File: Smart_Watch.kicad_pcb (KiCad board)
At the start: 4 copper layers, 32 x 32 mm, 52 parts, among them J1 2169900001, J2 Conn_01x02, J3 Conn_01x06, J4 Conn_01x02, SW2 SW_Push, SW3 SW_Push, SW4 SW_Push, SW5 SW_Push, SW6 SW_Push, SW7 SW_Push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

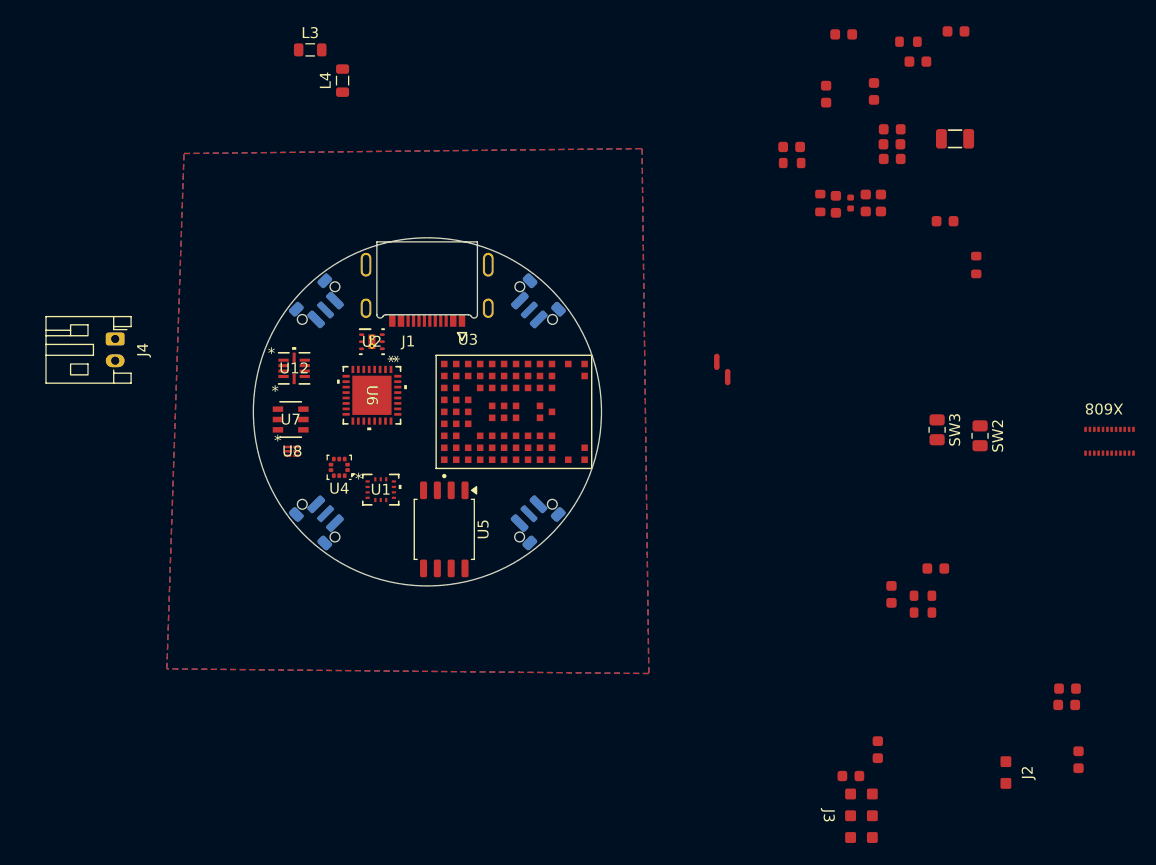
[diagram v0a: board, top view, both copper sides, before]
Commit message: Added Backpack Integration + Layout V1
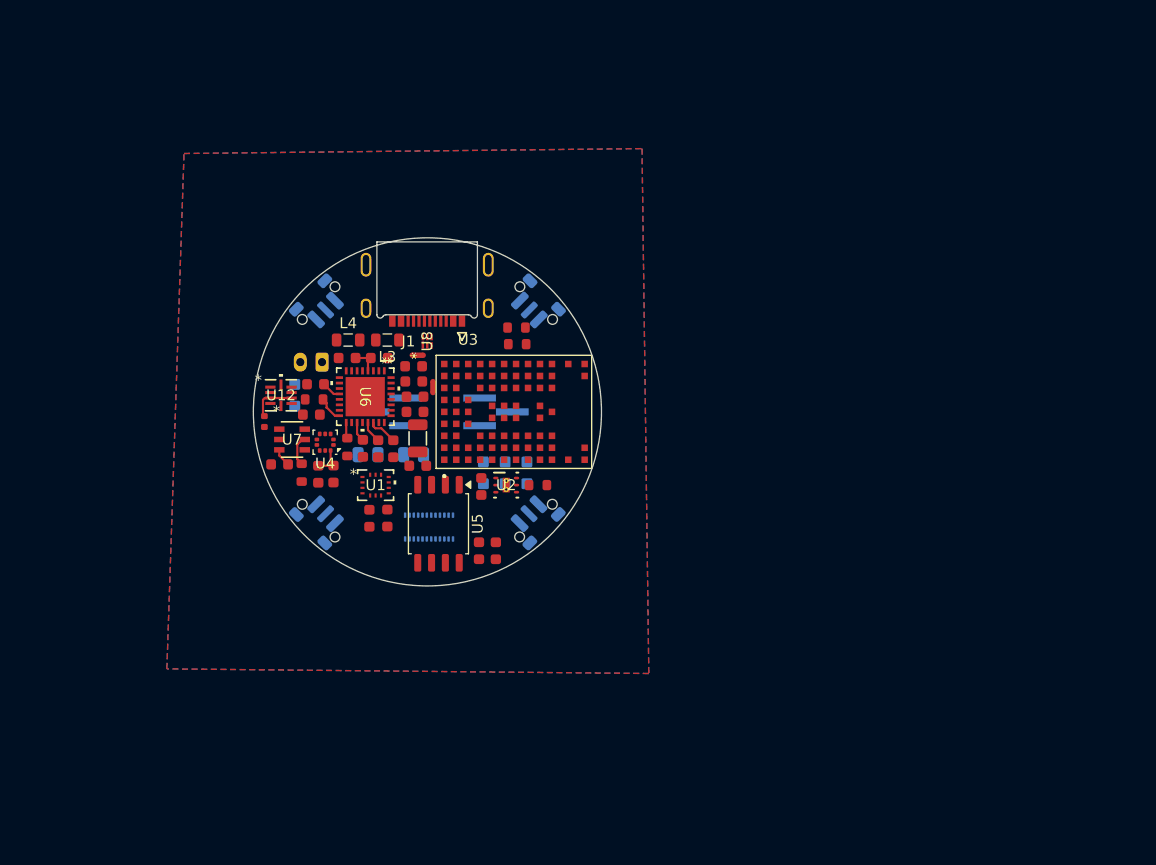
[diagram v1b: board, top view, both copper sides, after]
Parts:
- added J5: Conn_01x03, Connector_PinHeader_1.27mm:PinHeader_1x03_P1.27mm_Vertical_SMD_Pin1Left, B.Cu at (178.4, 107.8)
- added J6: Conn_01x03, Connector_PinHeader_1.27mm:PinHeader_1x03_P1.27mm_Vertical_SMD_Pin1Left, B.Cu at (168.7, 107.8)
- J2, J3, J4, SW2, SW3, X608: moved to B.Cu
- moved C23 77.3 mm to (161.5, 108.1), turned to 0 degrees
- moved J2 74.0 mm to (160.0, 106.3), turned to -90 degrees
- moved C14 65.1 mm to (158.6, 112.7)
- moved R11 64.9 mm to (160.6, 113.4)
- moved C24 63.6 mm to (171.3, 112.8)
- moved X608 63.0 mm to (172.3, 118.4)
- moved R9 57.5 mm to (157.2, 108.7)
- moved C8 57.3 mm to (162.1, 113.6), turned to -90 degrees
- moved X1 56.5 mm to (171.3, 110.3), turned to -90 degrees
- moved C25 56.3 mm to (171.0, 107.8)
- moved SW2 56.3 mm to (166.7, 111.8), turned to 180 degrees
- moved C26 55.6 mm to (176.9, 120.6), turned to 90 degrees
- moved C9 55.1 mm to (163.5, 113.6), turned to -90 degrees
- moved C21 54.4 mm to (178.4, 120.6), turned to 90 degrees
- moved C17 53.8 mm to (164.8, 102.9), turned to 180 degrees
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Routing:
- net VSYS: track 0.00 -> 6.93 mm
- net +1V8: track 0.00 -> 4.68 mm
- net /Architecture/MCU/ISET: track 0.00 -> 2.81 mm
- net /Architecture/MCU/VBUS_OUT: track 0.00 -> 2.71 mm
- net /Architecture/Power/VSET2: track 0.00 -> 2.38 mm
- net /Architecture/MCU/VBUS_IN: track 0.00 -> 2.02 mm
- net +BATT: track 0.00 -> 1.82 mm
- net +3V0: track 0.00 -> 1.67 mm
- net /Architecture/Power/VSET1: track 0.00 -> 1.48 mm

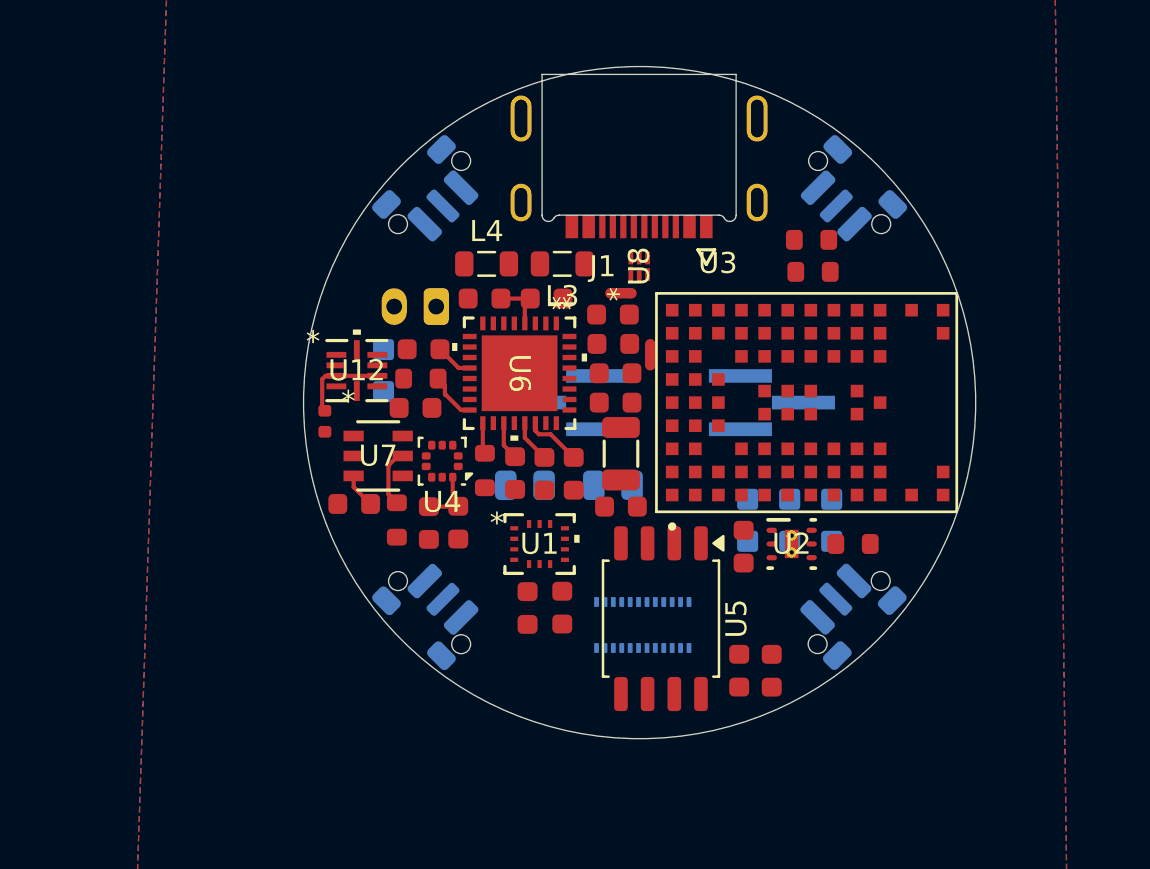
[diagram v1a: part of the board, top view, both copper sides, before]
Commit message: Layout Midpoint, Updated Backpack Schem
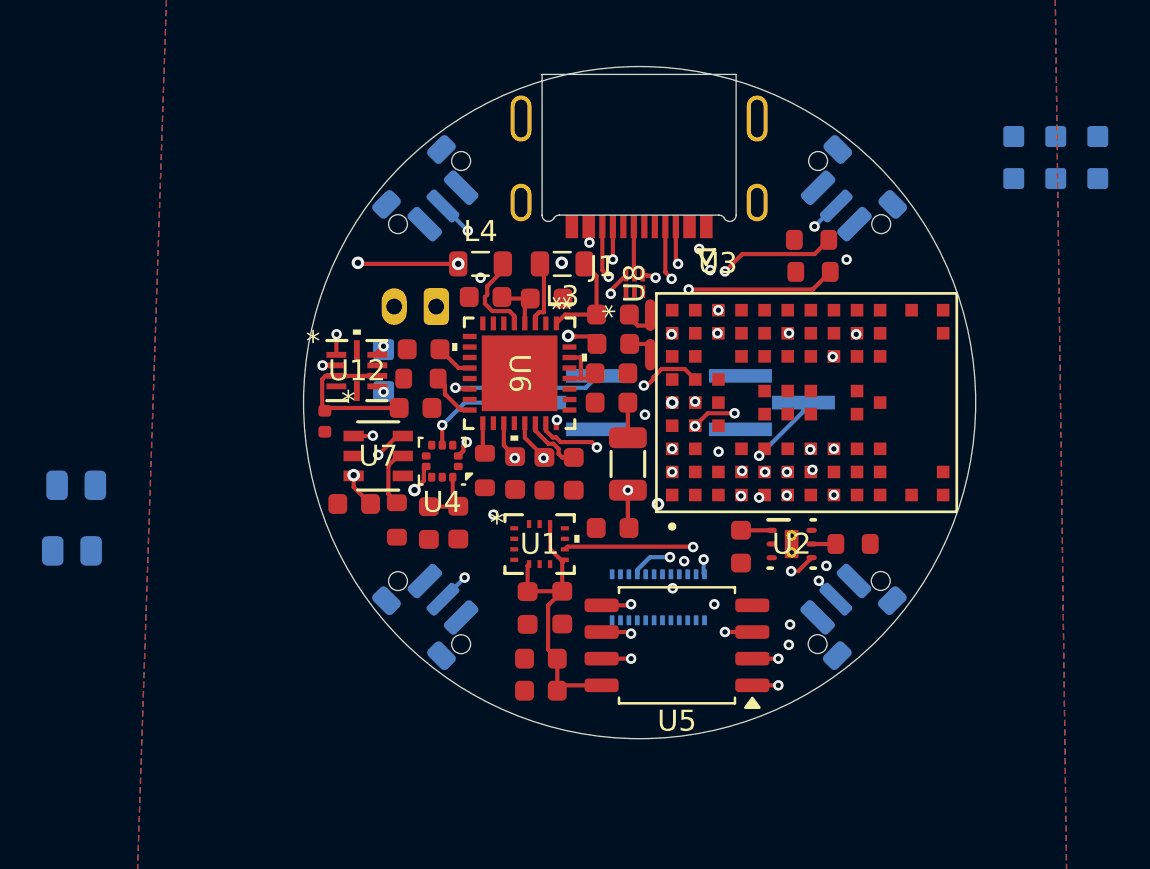
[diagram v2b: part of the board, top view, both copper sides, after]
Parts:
- moved SW3 25.9 mm to (145.1, 114.9)
- moved J3 21.4 mm to (192.0, 96.2)
- moved SW2 21.4 mm to (145.3, 111.8)
- moved C21 11.0 mm to (167.5, 121.6), turned to 180 degrees
- moved C26 9.46 mm to (167.5, 120.0), turned to 180 degrees
- moved NT1 1.74 mm to (172.7, 103.7), turned to 90 degrees
- moved X608 1.51 mm to (173.0, 117.1)
- moved U5 1.48 mm to (173.9, 119.4), turned to 180 degrees
- moved C24 1.09 mm to (170.9, 113.8)
- moved U8 0.84 mm to (171.9, 102.2)
- moved X1 0.59 mm to (171.6, 110.8)
- moved L4 0.29 mm to (164.6, 101.2)
- moved C18 0.20 mm to (170.8, 106.5)
- moved C25 0.20 mm to (170.8, 107.8)
- moved C7 0.13 mm to (177.0, 114.7)
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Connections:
- J5 pad 2: /Architecture/Peripherals/MAX_INT -> /Architecture/MCU/MAX_INT
- U3 pad A3: unconnected-(U3-P1.03/TWI-PadA3) -> /Architecture/MCU/SDA
- U3 pad B4: /Architecture/MCU/SDA -> /Architecture/MCU/SCL
- U3 pad C4: /Architecture/MCU/SCL -> unconnected-(U3-P1.01-PadC4)
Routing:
- net /Architecture/MCU/SCL: track 0.00 -> 39.4 mm, vias 0 -> 7
- net /Architecture/MCU/SDA: track 0.00 -> 32.5 mm, vias 0 -> 3
- net /Architecture/MCU/BTN_4: track 0.00 -> 31.1 mm, vias 0 -> 3
- net /Architecture/MCU/LRA_EN: track 0.00 -> 27.0 mm, vias 0 -> 2
- net /Architecture/MCU/PMIC_INT: track 0.00 -> 25.6 mm, vias 0 -> 2
- net /Architecture/MCU/LRA_PWM: track 0.00 -> 25.1 mm, vias 0 -> 2
- net +3V0: track 1.67 -> 26.7 mm, vias 0 -> 5
- net /Architecture/MCU/LEDK1: track 0.00 -> 24.5 mm, vias 0 -> 3
- net /Architecture/MCU/USB_RST: track 0.00 -> 23.8 mm, vias 0 -> 4
- net /Architecture/MCU/BTN_3: track 0.00 -> 21.9 mm, vias 0 -> 3
- net /Architecture/MCU/BTN_2: track 0.00 -> 20.8 mm, vias 0 -> 3
- net +1V8: track 4.68 -> 25.0 mm
- net /Architecture/MCU/LPS_INT: track 0.00 -> 18.3 mm, vias 0 -> 3
- net /Architecture/MCU/QSPI_IO3: track 0.00 -> 18.1 mm, vias 0 -> 3
- net /Architecture/MCU/VBUS_IN: track 2.02 -> 18.9 mm, vias 0 -> 3
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
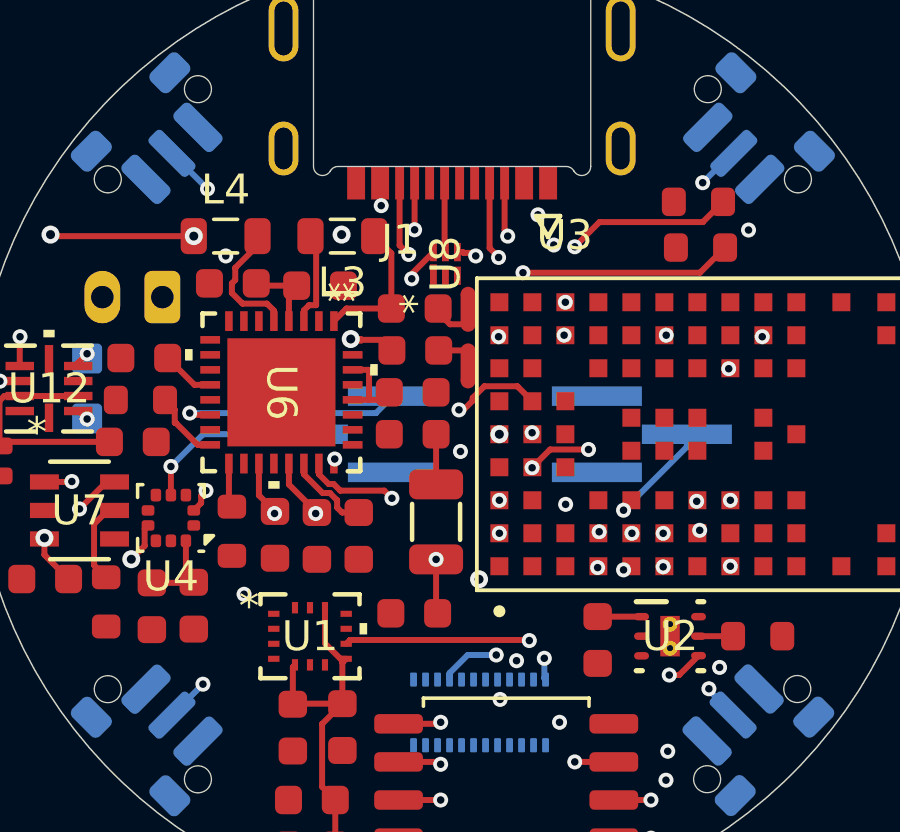
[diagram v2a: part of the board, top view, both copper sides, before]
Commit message: USB Layout Updates
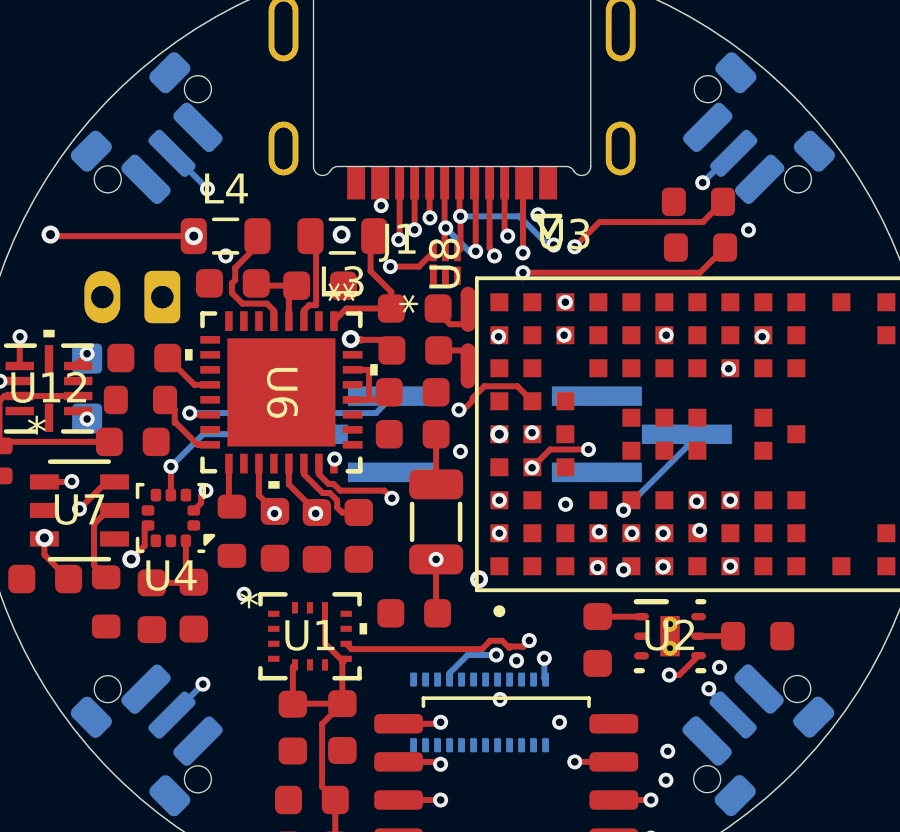
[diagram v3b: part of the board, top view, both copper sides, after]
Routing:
- net /Architecture/MCU/VBUS_IN: track 18.9 -> 25.1 mm, vias 3 -> 4
- net /Architecture/MCU/USBC_D-: track 2.32 -> 5.98 mm, vias 0 -> 2
- net /Architecture/MCU/USBC_D+: track 8.33 -> 10.4 mm, vias 3 -> 4
- net /Architecture/MCU/LRA_EN: track 27.0 -> 26.2 mm
- net /Architecture/MCU/USB_RST: track 23.8 -> 24.5 mm

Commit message: Routing V1 Complete!
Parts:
- moved SW3 39.3 mm to (184.4, 113.0), turned to 180 degrees
- moved SW2 19.4 mm to (164.7, 111.6)
- moved J3 14.4 mm to (179.0, 102.5)
- moved C11 0.24 mm to (166.2, 111.4)
- moved R2 0.20 mm to (180.5, 100.1)
- moved R1 0.13 mm to (180.5, 101.6)
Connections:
- U2 pad V: (no net) -> GND
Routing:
- net +1V8: track 25.1 -> 83.1 mm, vias 0 -> 7
- net /Architecture/MCU/SDA: track 32.5 -> 73.1 mm, vias 3 -> 9
- net /Architecture/MCU/DISPLAY_RST: track 0.00 -> 28.3 mm, vias 0 -> 3
- net /Architecture/MCU/SCL: track 39.4 -> 65.7 mm, vias 7 -> 10
- net VSYS: track 13.6 -> 39.6 mm, vias 0 -> 4
- net +3V0: track 26.7 -> 50.3 mm, vias 5 -> 7
- net /Architecture/MCU/DISPLAY_LIGHT_IO: track 0.92 -> 23.2 mm
- net GND: track 0.00 -> 22.1 mm, vias 0 -> 34
- net /Architecture/MCU/LEDK2: track 0.00 -> 19.5 mm, vias 0 -> 4
- net /Architecture/MCU/CTP_RST: track 0.00 -> 18.2 mm, vias 0 -> 3
- net /Architecture/MCU/VBUS_OUT: track 2.85 -> 19.6 mm, vias 0 -> 4
- net /Architecture/MCU/MCU_RST: track 0.00 -> 15.1 mm, vias 0 -> 3
- net /Architecture/MCU/OPT_INT: track 1.15 -> 16.1 mm, vias 0 -> 3
- net /Architecture/MCU/SWCLK: track 0.00 -> 14.2 mm, vias 0 -> 3
- net /Architecture/MCU/CTP_INT: track 0.00 -> 11.6 mm, vias 0 -> 3
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
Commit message: PCB V1 Complete!
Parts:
- added G***: LOGO, LOGO, B.Cu at (171.2, 102.2)
- added G***: LOGO, LOGO, B.Cu at (168.7, 114.7)
